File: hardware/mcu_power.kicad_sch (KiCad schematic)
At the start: 85 parts, among them Q201 MMBT3904, Q202 IRLML2244, SW201 Button Power, SW202 Reset, SW203 Button Enter, SW204 Button Left, SW205 Button Up, SW206 Button Down, SW207 Button Escape, SW208 Button Right, U201 STM32F405RGTx, U202 TPS7A2033, U203 TP6841S6, Y201 8 MHz

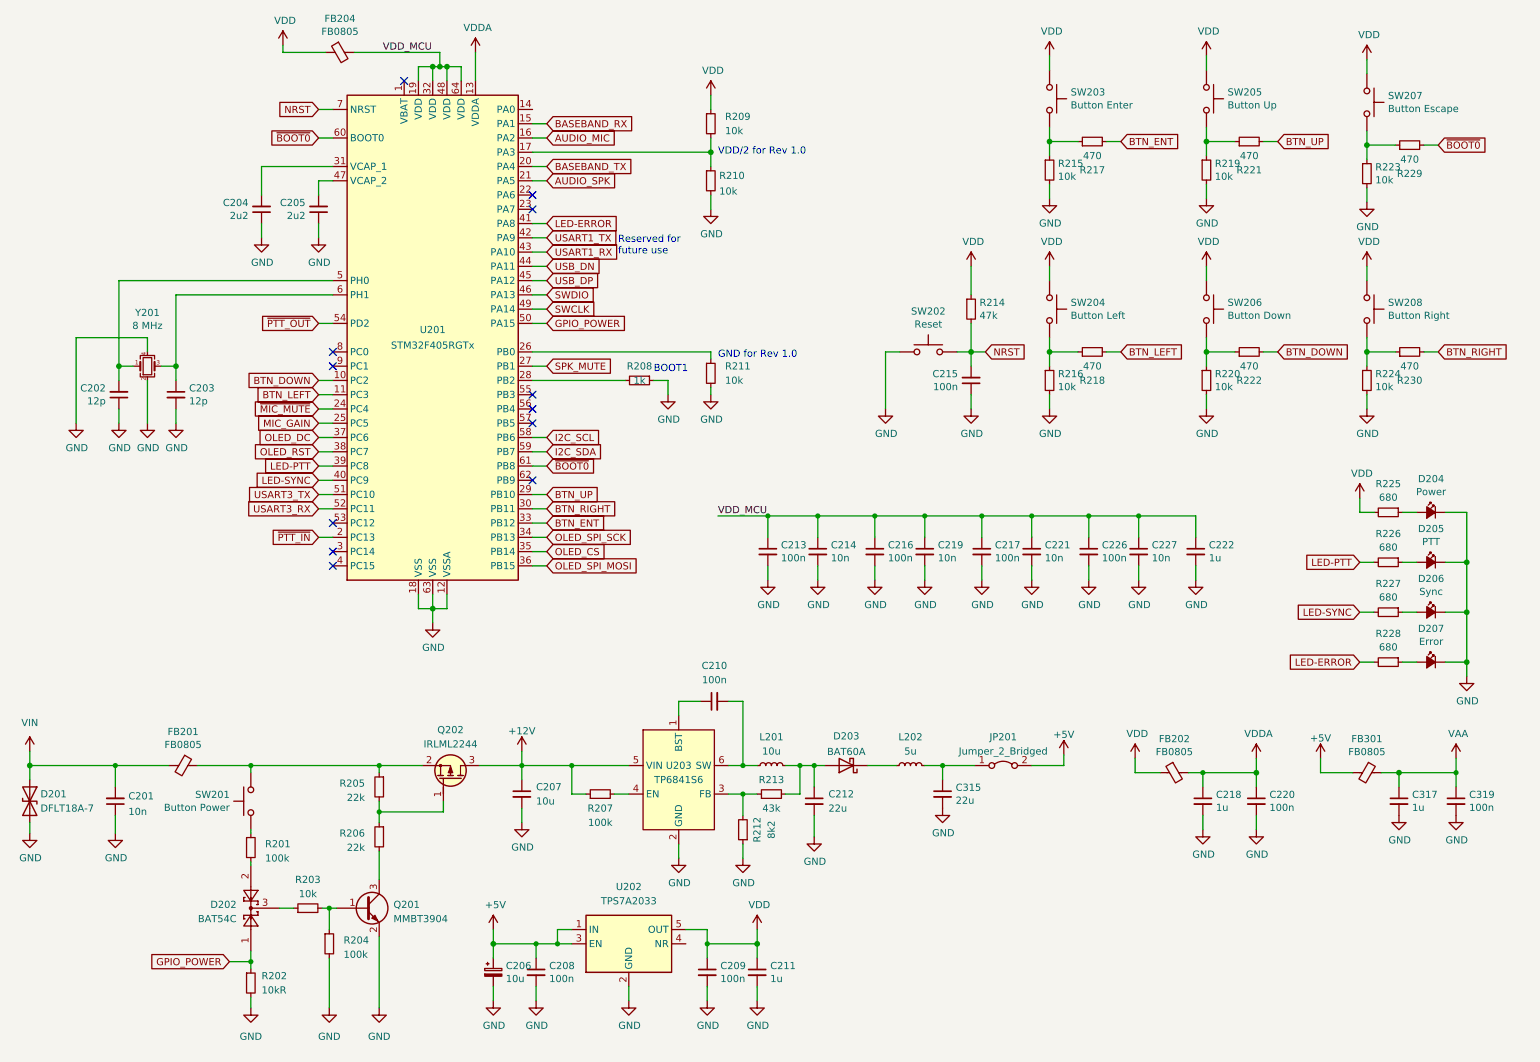
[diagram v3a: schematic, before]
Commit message: PCB Layout [WIP] + HMI connector
Added ZIF connector for HMI, updated reset button reference, added backup power connector for RTC + general layout progress
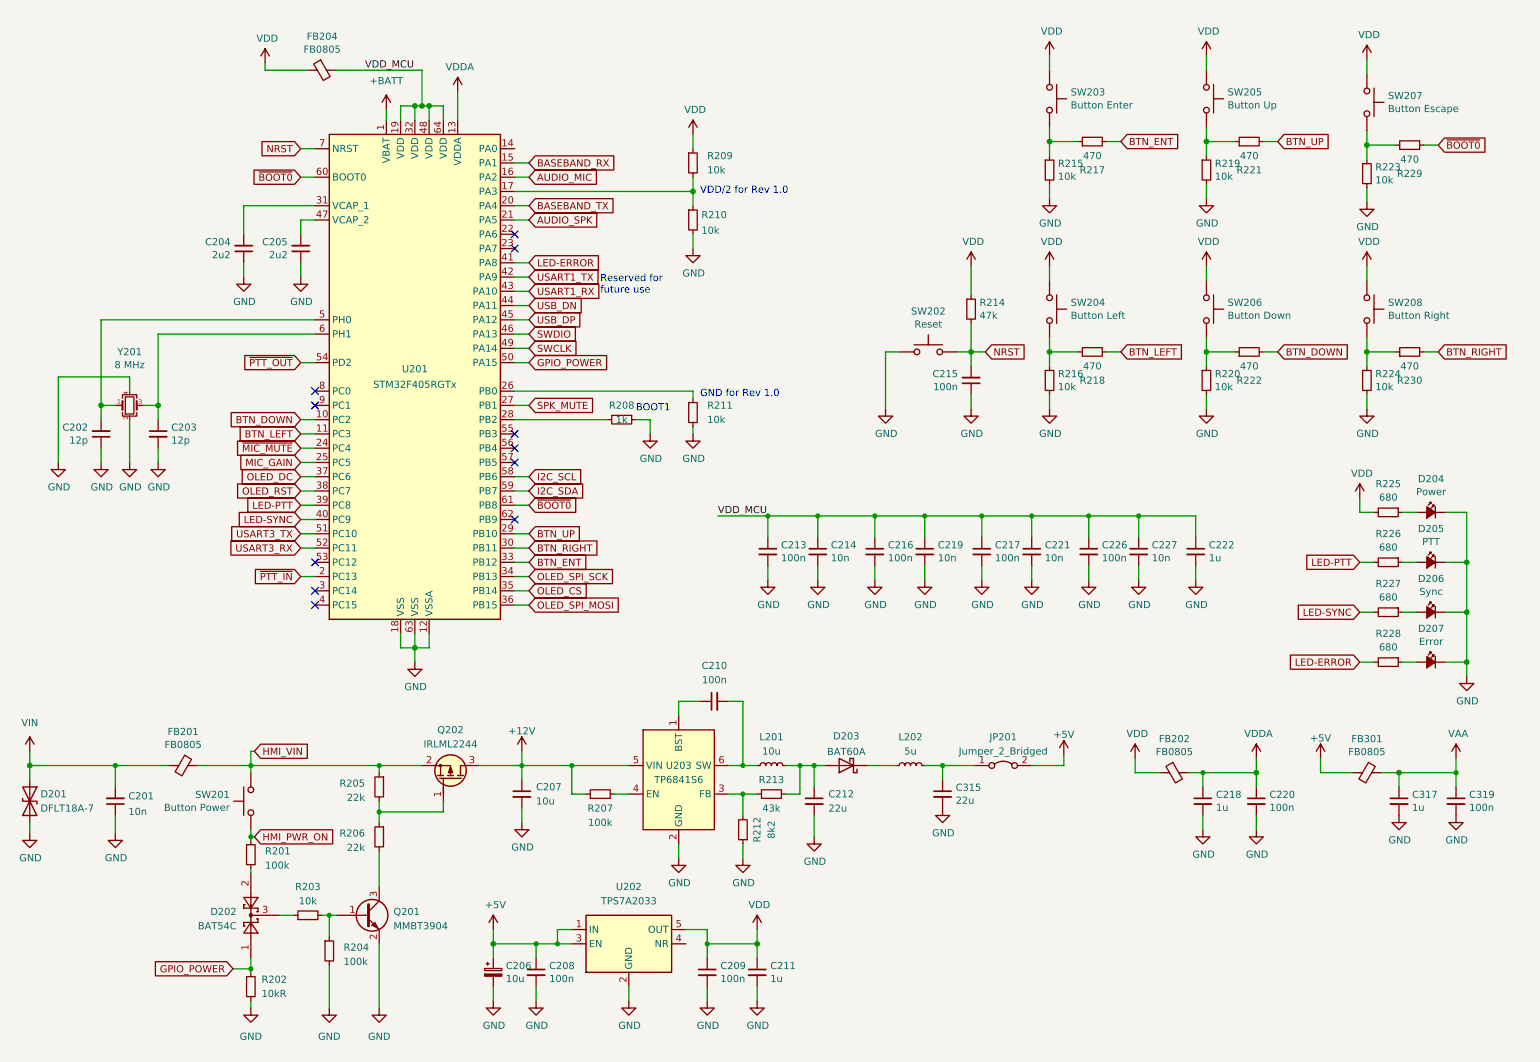
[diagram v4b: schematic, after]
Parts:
- SW202: footprint pkl_buttons_switches:SW_SPST_3x4x2.5 -> M17_misc_passive:SW_SPST_436351045816; LCSC Part # C221895 -> C79174; MPN PTS810SJG250SMTRLFS -> EVQPUC02K
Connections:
- net GND: now also SW202.2; no longer SW202.1
- net NRST: now also SW202.1; no longer SW202.2
- net HMI_VIN: now reaches FB201.1, Q202.2 (S), R205.1, SW201.1
- net HMI_PWR_ON: now reaches R201.1, SW201.2
- net +BATT: now reaches U201.1 (VBAT)
- no-connect marks 12 -> 11
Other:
- moved on the sheet: C202, C203, C204, C205, D202, FB204, Q201, R201, R202, R203, R204, R208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

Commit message: Replaced pkl symbols with kicad library symbols
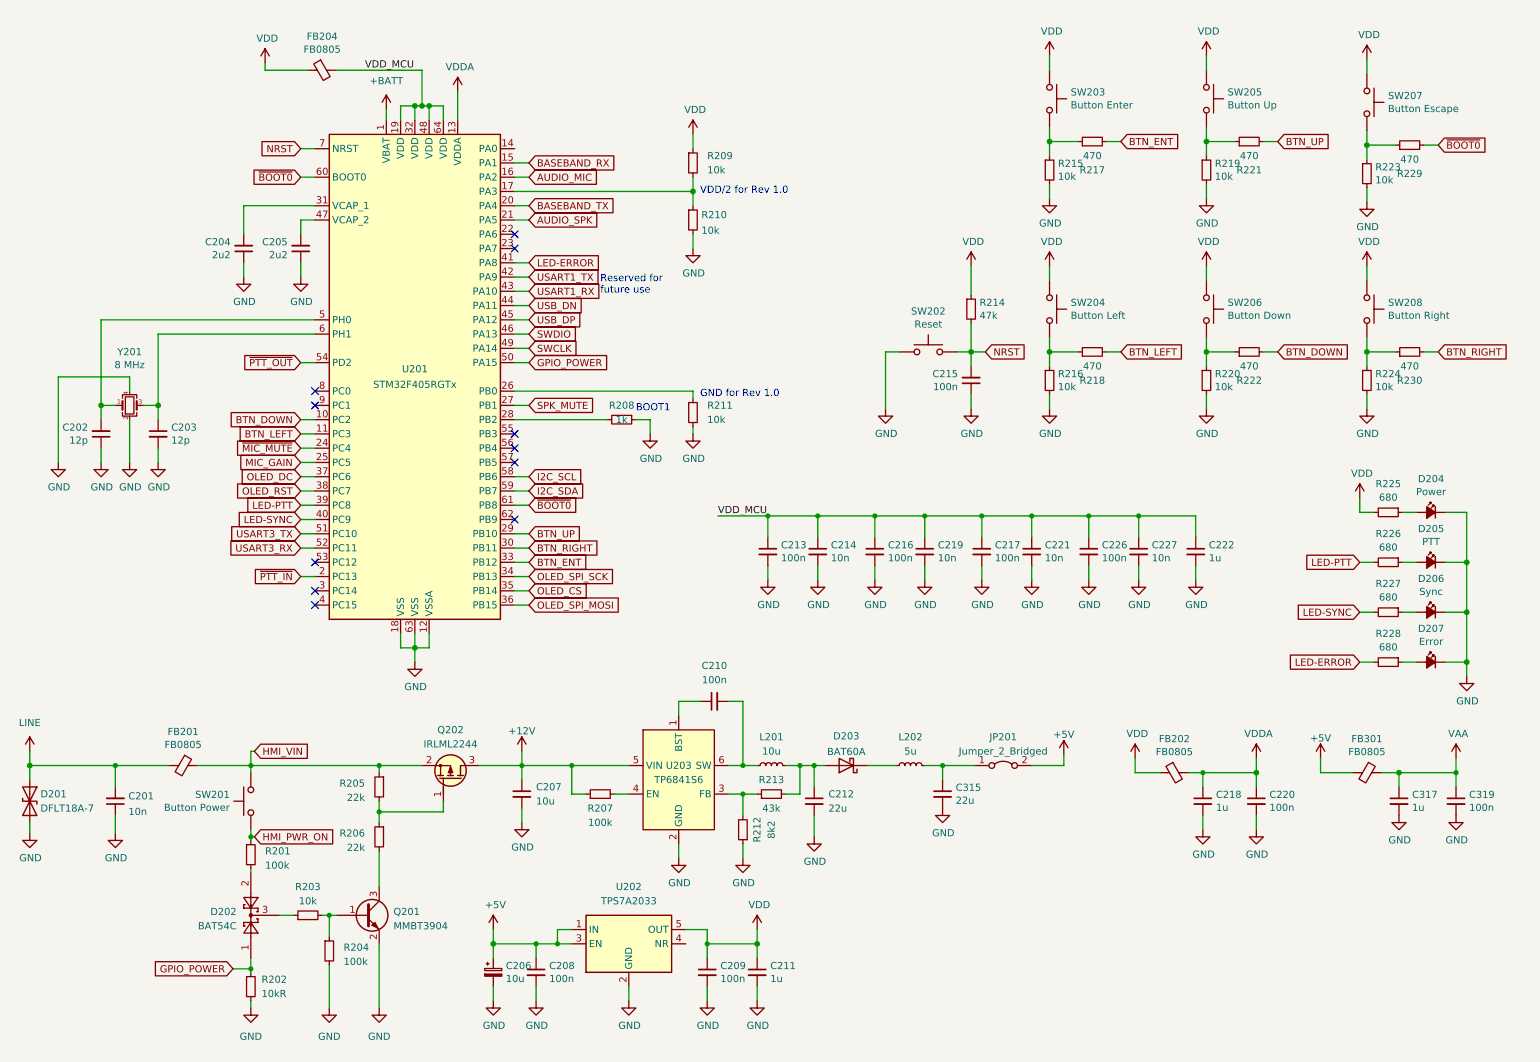
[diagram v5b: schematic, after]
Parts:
- C201, C202, C203, C204, C205, C207, C208, C209, C210, C211, C212, C213, C214, C215, C216, C217, C218, C219, C220, C221, C222, C226, C227, C315, C317, C319: symbol pkl_device:pkl_C_Small -> Device:C_Small
- C206: symbol pkl_device:pkl_CP_Small -> Device:C_Polarized_Small
- D204, D205, D206, D207: symbol pkl_device:pkl_Led_Small -> Device:LED_Small_Filled
- L201, L202: symbol pkl_device:pkl_L_Small -> Device:L_Small
- R207, R208, R209, R210, R211, R212, R213, R214, R215, R216, R217, R218, R219, R220, R221, R222, R223, R224, R225, R226, R227, R228, R229, R230: symbol pkl_device:pkl_R_Small -> Device:R_Small
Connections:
- net GND: now also D204.1 (K), D205.1 (K), D206.1 (K), D207.1 (K); no longer D204.C, D205.C, D206.C, D207.C
- net at R225.1: now also D204.2 (A); no longer D204.A
- net at R226.1: now also D205.2 (A); no longer D205.A
- net at R227.1: now also D206.2 (A); no longer D206.A
- net at R228.1: now also D207.2 (A); no longer D207.A
- net VIN renamed LINE
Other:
- moved on the sheet: L201, L202

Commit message: Replaced pkl footprints with kicad standard library footprints
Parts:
- C201, C202, C203, C204, C205, C208, C209, C210, C211, C213, C214, C215, C216, C217, C218, C219, C220, C221, C222, C226, C227, C315, C317, C319: footprint pkl_dipol:C_0603 -> Capacitor_SMD:C_0603_1608Metric
- D204, D205, D206, D207: footprint pkl_dipol:D_0603 -> LED_SMD:LED_0603_1608Metric
- FB201, FB202, FB204, FB301, L202: footprint pkl_dipol:L_0805 -> Inductor_SMD:L_0805_2012Metric
- R201, R202, R203, R204, R205, R206, R207, R208, R209, R210, R211, R212, R213, R214, R215, R216, R217, R218, R219, R220, R221, R222, R223, R224, R225, R226, R227, R228, R229, R230: footprint pkl_dipol:R_0603 -> Resistor_SMD:R_0603_1608Metric
- SW201, SW203, SW204, SW205, SW206, SW207, SW208: footprint pkl_buttons_switches:SW_SPST_PTS645 -> Button_Switch_SMD:SW_SPST_PTS645

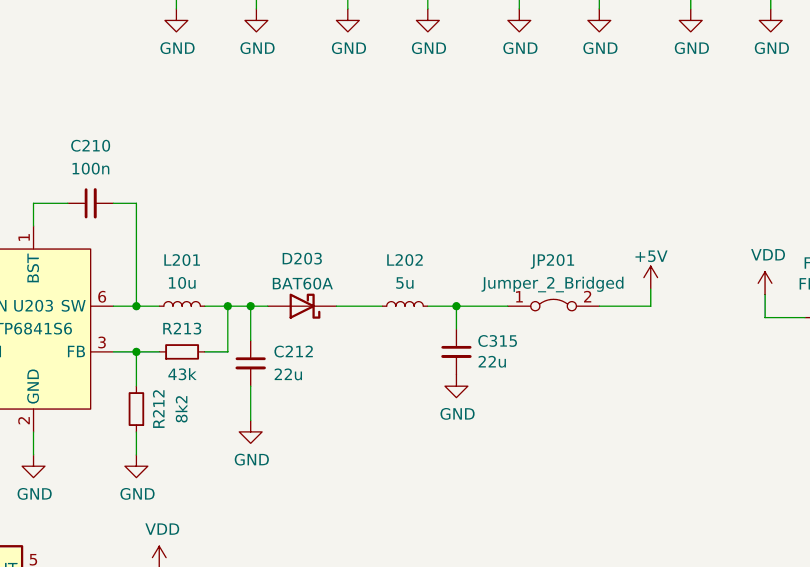
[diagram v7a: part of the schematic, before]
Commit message: Updated power supply low pass filter
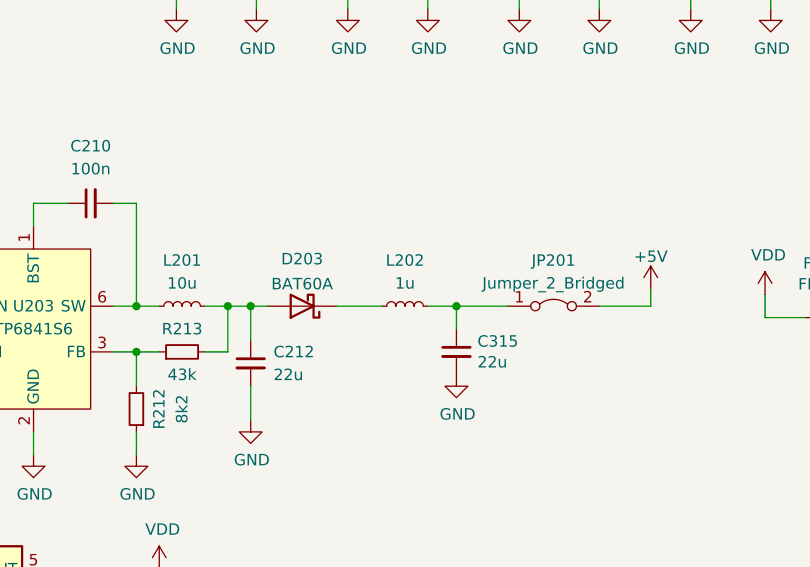
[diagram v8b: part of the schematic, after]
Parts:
- C315: footprint Capacitor_SMD:C_0603_1608Metric -> Capacitor_SMD:C_1206_3216Metric; MPN Generic C/22uF/C0G/10V/0603 -> Generic C/22uF/X7R/10V/1206
- L202: value 5u -> 1u; LCSC Part # C506573 -> (none); MPN Generic L/5u/0805/1A -> Generic L/1u/0805/1A
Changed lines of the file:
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@@
       (effects (font (size 1.27 1.27)) (justify left))
     )
-    (property "Footprint" "Capacitor_SMD:C_0603_1608Metric" (at 182.245 151.13 0)
+    (property "Footprint" "Capacitor_SMD:C_1206_3216Metric" (at 182.245 151.13 0)
       (effects (font (size 1.524 1.524)) hide)
     )
@@
       (effects (font (size 1.524 1.524)))
     )
-    (property "MPN" "Generic C/22uF/C0G/10V/0603" (at 182.245 151.13 0)
+    (property "MPN" "Generic C/22uF/X7R/10V/1206" (at 182.245 151.13 0)
       (effects (font (size 1.27 1.27)) hide)
     )
@@
       (effects (font (size 1.27 1.27)))
     )
-    (property "Value" "5u" (at 176.53 143.51 90)
+    (property "Value" "1u" (at 176.53 143.51 90)
       (effects (font (size 1.27 1.27)))
     )
@@
       (effects (font (size 1.524 1.524)))
     )
-    (property "MPN" "Generic L/5u/0805/1A" (at 176.53 146.05 0)
-      (effects (font (size 1.27 1.27)) hide)
-    )
-    (property "LCSC Part #" " C506573" (at 176.53 146.05 0)
-      (effects (font (size 1.27 1.27)) hide)
-    )
+    (property "MPN" "Generic L/1u/0805/1A" (at 176.53 146.05 0)
+      (effects (font (size 1.27 1.27)) hide)
+    )
+    (property "LCSC Part #" "" (at 176.53 146.05 0)
+      (effects (font (size 1.27 1.27)) hide)
+    )
